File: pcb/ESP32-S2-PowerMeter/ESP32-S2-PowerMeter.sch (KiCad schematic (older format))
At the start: 66 parts, among them J1 USB_C_Receptacle_USB2.0, J2 Battery, J3 AudioJack3, J4 AudioJack3, J5 AudioJack3, J6 AudioJack3, J7 AC In, SW1 SW_SPDT, SW2 SW_DIP_x02, SW3 SW_DIP_x02, U1 ESP32-S2-WROVER, U2 XC6806XXXX11-G, U3 XC6203E332PR, U4 CJ432, U5 LM741

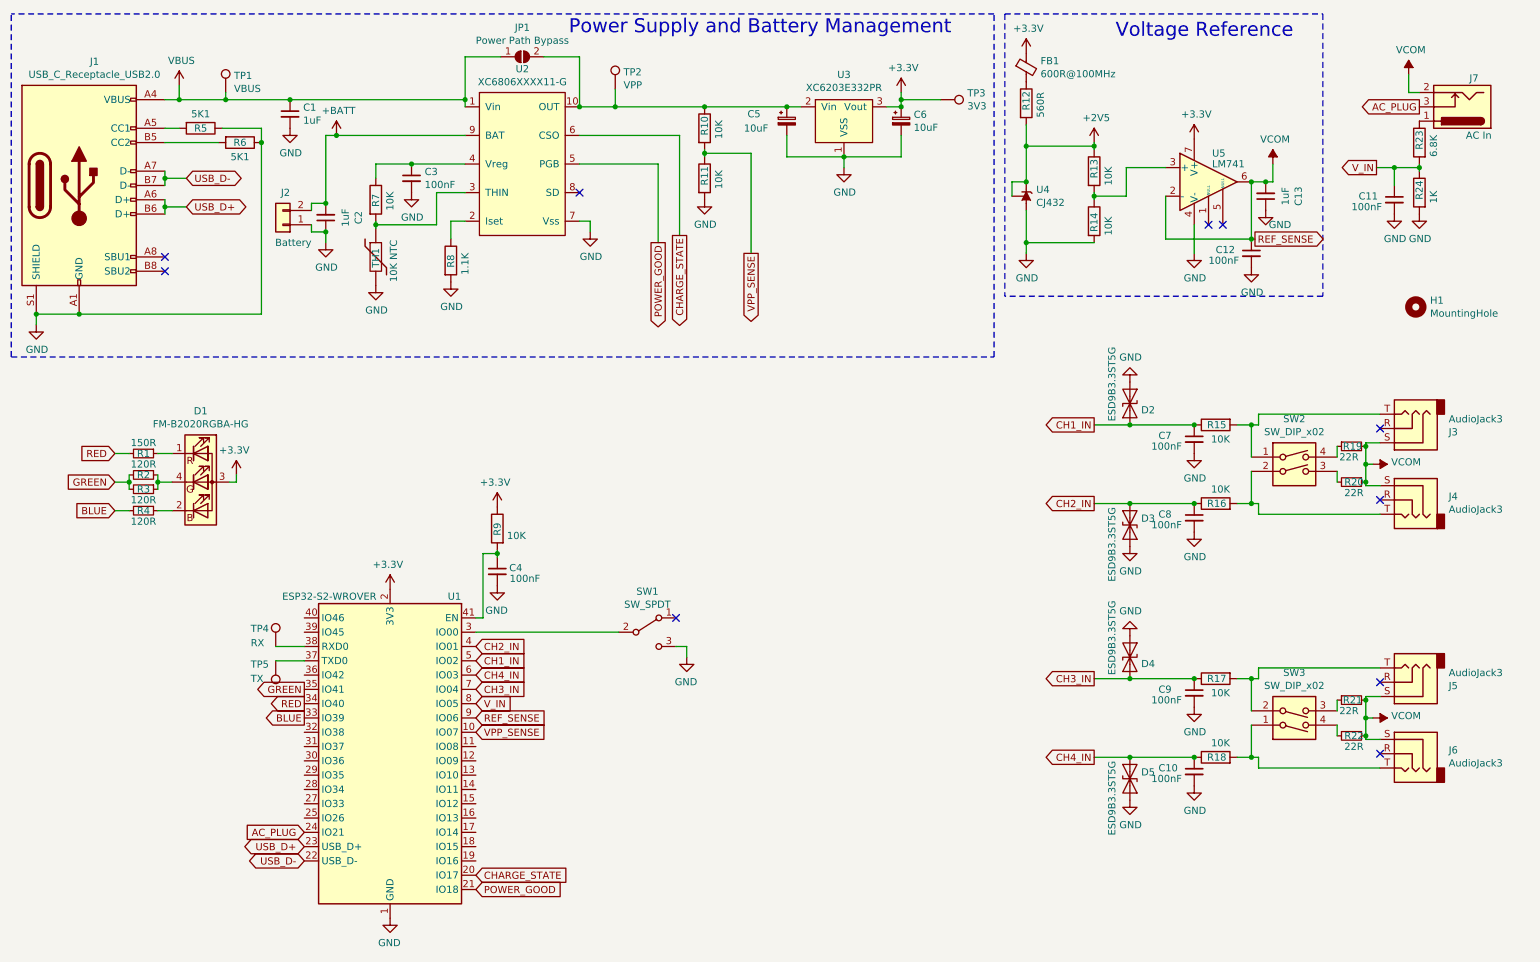
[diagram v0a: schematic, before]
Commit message: Updated schematic - Added ESD diodes to USB and V sense - Fixed V sense input to be reference centered - Added jumper to choose between CJ431 and CJ432 - Replaced XC6806 with JLC assemble-able BQ24074 - Moved battery sense to battery rather then the power path
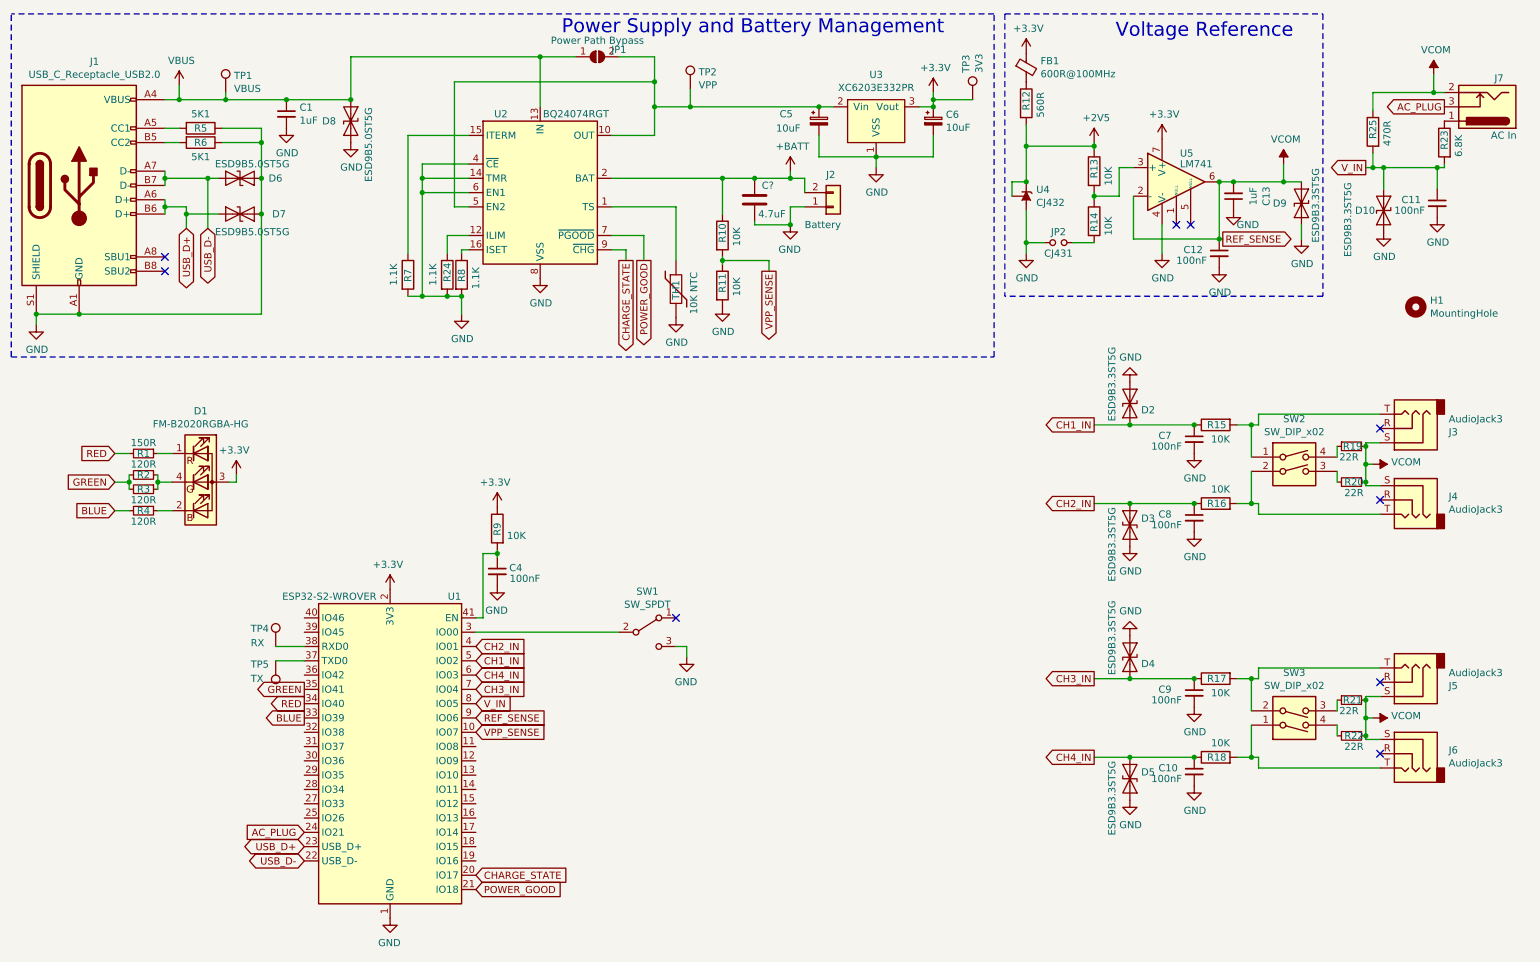
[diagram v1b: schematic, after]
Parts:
- removed C2: 1uF, Capacitor_SMD:C_0603_1608Metric, symbol Device:C_Small
- removed C3: 100nF, Capacitor_SMD:C_0402_1005Metric, symbol Device:C_Small
- removed U2: XC6806XXXX11-G, project:LGA-10B01, symbol xc6806xxxx11-g:XC6806XXXX11-G
- added C?: 4.7uF, Capacitor_SMD:C_0603_1608Metric, symbol Device:C
- added D10, D9: ESD9B3.3ST5G, project:SMD-DFN1006, symbol Diode:ESD9B3.3ST5G
- added D6, D7, D8: ESD9B5.0ST5G, project:SMD-DFN1006, symbol Diode:ESD9B3.3ST5G
- added JP2: CJ431, Jumper:SolderJumper-2_P1.3mm_Open_RoundedPad1.0x1.5mm, symbol Device:Jumper_NO_Small
- added R25: 470R, Resistor_SMD:R_0402_1005Metric, symbol Device:R
- added U2: BQ24074RGT, Package_DFN_QFN:VQFN-16-1EP_3x3mm_P0.5mm_EP1.6x1.6mm, symbol Battery_Management:BQ24074RGT
- R24: value 1K -> 1.1K; LCSC Part C11702 -> C25860
- R7: value 10K -> 1.1K; LCSC Part C25744 -> C25860
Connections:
- net +BATT: now also R10.1, C?.1, U2.2 (BAT), U2.3 (BAT)
- net CHARGE_STATE: now also U2.9 (~CHG)
- net GND: now also R7.2, C?.2, D10.1 (A1), D6.2 (A2), D7.2 (A2), D8.1 (A1), D9.1 (A1), JP2.1, U2.14 (TMR), U2.17 (VSS), U2.4 (~CE), U2.6 (EN1), U2.8 (VSS); no longer R14.2
- net POWER_GOOD: now also U2.7 (~PGOOD)
- net USB_D+: now also D7.1 (A1)
- net USB_D-: now also D6.1 (A1)
- net VBUS: now also D8.2 (A2), U2.13 (IN)
- net VCOM: now also D9.2 (A2), R25.1
- net V_IN: now also D10.2 (A2), R25.2; no longer R24.1
- net at C5.1, JP1.2 (B), TP2.1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: now also U2.10 (OUT), U2.11 (OUT), U2.5 (EN2); no longer R10.1
- net at R8.1: now also U2.16 (ISET)
- net at TH1.1: now also U2.1 (TS); no longer R7.2
- net at R7.1: now also U2.15 (ITERM)
- new net: JP2.2, R14.2
- new net: R24.1, U2.12 (ILIM)
- no-connect marks 10 -> 9
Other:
- moved on the sheet: C1, C11, C12, C13, C5, C6, J2, J7, JP1, R10, R11, R23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
